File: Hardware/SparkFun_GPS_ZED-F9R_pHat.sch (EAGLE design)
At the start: 77 parts, among them J1 U.FL, J5 QWIIC_RIGHT_ANGLE, J6 RASPBERRYPI-40-PIN-GPIO_SMD_S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, U1 U-BLOX_ZED_F9R, U2 DUAL-OPTO_HCPL-073L, U3 UHS_INVERTER_SCHMITT_TRIGGERS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, U4 UHS_INVERTER_SCHMITT_TRIGGERS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

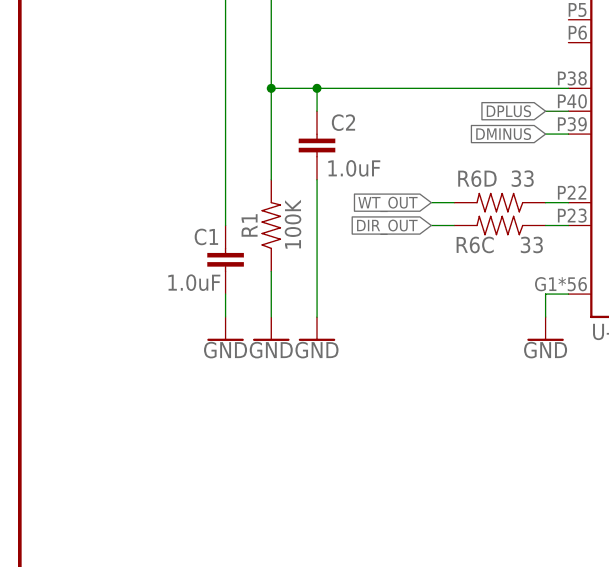
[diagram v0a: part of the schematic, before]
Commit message: Replaces 6.3V rated 0.1uF caps with 10V rated ones
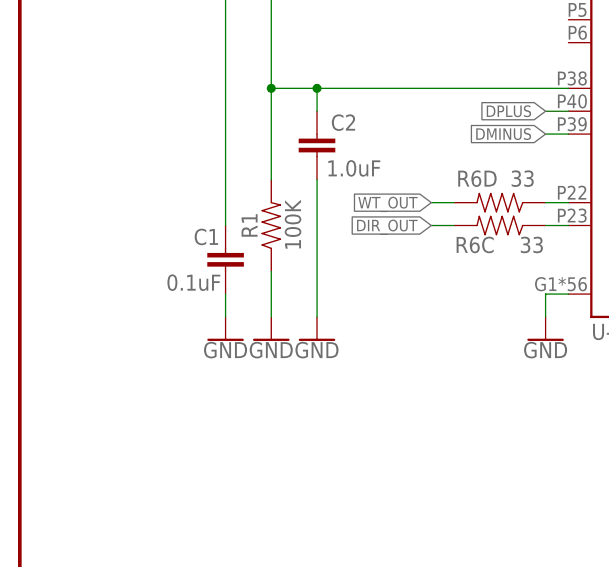
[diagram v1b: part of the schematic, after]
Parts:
- C1: value 1.0uF -> 0.1uF; device SparkFun-Capacitors:1.0UF-0402-16V-10% -> SparkFun-Capacitors:0.1UF-0402-10V-10%-X7R
- C4, C7, C8: device SparkFun-Capacitors:0.1UF-0402-6.3V-10%-X7R -> SparkFun-Capacitors:0.1UF-0402-10V-10%-X7R
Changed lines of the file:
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@@
 <part name="FRAME1" library="SparkFun-Aesthetics" deviceset="FRAME-LEDGER" device=""/>
 <part name="C3" library="SparkFun-Capacitors" deviceset="47PF" device="-0402-25V-5%-X7R" value="47pF"/>
-<part name="C1" library="SparkFun-Capacitors" deviceset="1.0UF" device="-0402-16V-10%" value="1.0uF"/>
+<part name="C1" library="SparkFun-Capacitors" deviceset="0.1UF" device="-0402-10V-10%-X7R" value="0.1uF"/>
 <part name="D6" library="SparkFun-IC-Power" deviceset="PRTR5V0U2" device="F"/>
 <part name="SUPPLY14" library="SparkFun-PowerSymbols" deviceset="3.3V" device=""/>
@@
 <part name="R22" library="SparkFun-Resistors" deviceset="910OHM" device="-0603-1/10W-5%" value="910"/>
 <part name="U2" library="SparkFun-DiscreteSemi" deviceset="DUAL-OPTO_HCPL-073L" device=""/>
-<part name="C4" library="SparkFun-Capacitors" deviceset="0.1UF" device="-0402-6.3V-10%-X7R" value="0.1uF"/>
+<part name="C4" library="SparkFun-Capacitors" deviceset="0.1UF" device="-0402-10V-10%-X7R" value="0.1uF"/>
 <part name="SUPPLY9" library="SparkFun-PowerSymbols" deviceset="3.3V" device=""/>
 <part name="GND11" library="SparkFun-PowerSymbols" deviceset="GND" device=""/>
@@
 <part name="SUPPLY12" library="SparkFun-PowerSymbols" deviceset="3.3V" device=""/>
 <part name="SUPPLY13" library="SparkFun-PowerSymbols" deviceset="3.3V" device=""/>
-<part name="C7" library="SparkFun-Capacitors" deviceset="0.1UF" device="-0402-6.3V-10%-X7R" value="0.1uF"/>
-<part name="C8" library="SparkFun-Capacitors" deviceset="0.1UF" device="-0402-6.3V-10%-X7R" value="0.1uF"/>
+<part name="C7" library="SparkFun-Capacitors" deviceset="0.1UF" device="-0402-10V-10%-X7R" value="0.1uF"/>
+<part name="C8" library="SparkFun-Capacitors" deviceset="0.1UF" device="-0402-10V-10%-X7R" value="0.1uF"/>
 <part name="GND21" library="SparkFun-PowerSymbols" deviceset="GND" device=""/>
 <part name="TP6" library="SparkFun-Connectors" deviceset="TEST-POINT" device="3X4" value="TEST-POINT3X4"/>

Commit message: Replaces one of the .1uF with a 1uF Capacitor
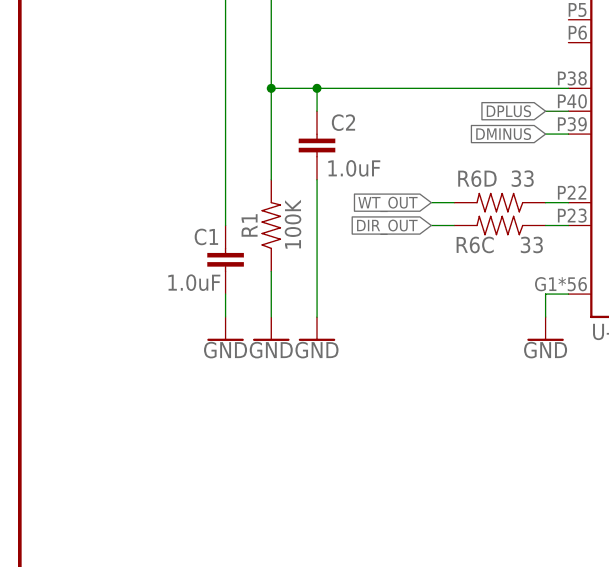
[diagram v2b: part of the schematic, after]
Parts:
- C1: value 0.1uF -> 1.0uF; device SparkFun-Capacitors:0.1UF-0402-10V-10%-X7R -> SparkFun-Capacitors:1.0UF-0402-16V-10%
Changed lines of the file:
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@@
 <part name="FRAME1" library="SparkFun-Aesthetics" deviceset="FRAME-LEDGER" device=""/>
 <part name="C3" library="SparkFun-Capacitors" deviceset="47PF" device="-0402-25V-5%-X7R" value="47pF"/>
-<part name="C1" library="SparkFun-Capacitors" deviceset="0.1UF" device="-0402-10V-10%-X7R" value="0.1uF"/>
+<part name="C1" library="SparkFun-Capacitors" deviceset="1.0UF" device="-0402-16V-10%" value="1.0uF"/>
 <part name="D6" library="SparkFun-IC-Power" deviceset="PRTR5V0U2" device="F"/>
 <part name="SUPPLY14" library="SparkFun-PowerSymbols" deviceset="3.3V" device=""/>
